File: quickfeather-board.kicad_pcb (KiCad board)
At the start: 4 copper layers, 58.4 x 22.9 mm, 100 parts, among them IC1 EOS-S3-QFN, J1 61300211121, J2 1x12_pinhead, J3 1x16_pinhead, J4 S2B-PH-SM4-TB_LF__SN_, J5 0473460001, J6 FTSH-105-01-L-DV-K, J7 61300211121, J8 2x8_pinhead, M1 mounting_pad, M2 mounting_pad, M3 mounting_pad, M4 mounting_pad, Q1 NX3008CBKV, Q2 2N7002PV, Q3 2N7002PV, Q4 DMG1012T-7, U1 TPS62821DLCR, U2 MCP73831T-2ACI_OT, U3 GD25Q16CWIGR, U4 DPS310, U5 MC3635, X1 ECS-_327-12_5-34B-TR

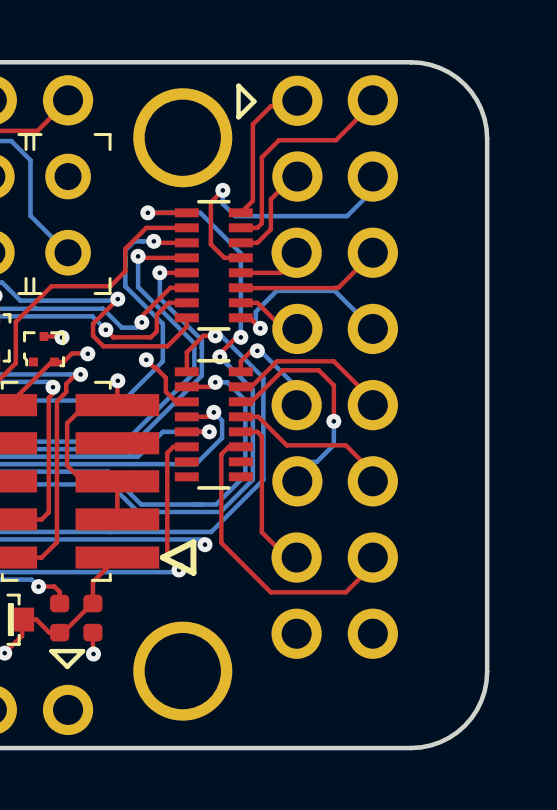
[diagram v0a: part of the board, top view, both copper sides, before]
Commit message: Add board name to TOP silkscreen
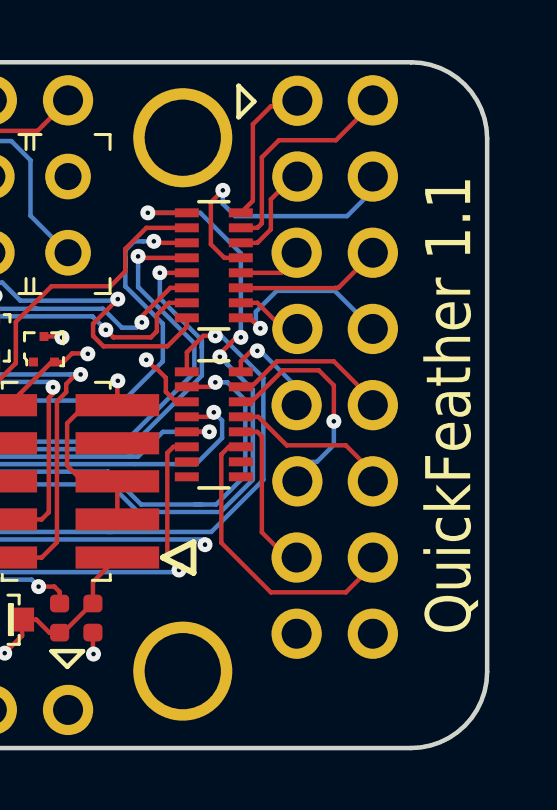
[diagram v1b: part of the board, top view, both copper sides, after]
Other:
- board text added: "QuickFeather 1.1"
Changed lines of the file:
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@@
   (general
     (thickness 1.6)
-    (drawings 108)
+    (drawings 110)
     (tracks 1938)
     (zones 0)
@@
     (34 B.Paste user hide)
     (35 F.Paste user hide)
-    (36 B.SilkS user)
-    (37 F.SilkS user hide)
+    (36 B.SilkS user hide)
+    (37 F.SilkS user)
     (38 B.Mask user hide)
     (39 F.Mask user hide)
@@
     )
   )
+  (gr_text "QuickFeather 1.1" (at 180.2603 105.0036 90) (layer F.SilkS)
+    (effects (font (size 1.5 1.3) (thickness 0.2)))
+  )
+  (gr_line (start 179 94.7717) (end 179 113.3417) (layer F.Fab) (width 0.15))
   (gr_text Prepreg (at 209.601 111.243) (layer Dwgs.User)
     (effects (font (size 1 1) (thickness 0.15)))
